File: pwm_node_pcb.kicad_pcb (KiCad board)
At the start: 4 copper layers, 40 x 35 mm, 49 parts, among them J1 Battery, J2 5V Breakout, J3 TC2050-IDC-NL, J4 CAN1, J5 Load Source, U1 LMR51430, U2 LD1117S33CTR, U3 TJA1051T/3, U4 STM32L432KCU, U5 TXB0104QPWRQ1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

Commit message: Fix level shifter circuit
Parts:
- moved C14 6.89 mm to (148.3, 111.3), turned to -90 degrees
- moved C15 6.41 mm to (148.3, 115.3), turned to 90 degrees
- moved U5 1.75 mm to (144.8, 113.3), turned to -90 degrees
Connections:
- C14 pad 1: +5V -> +3V3
- C15 pad 1: +3V3 -> +5V
- U5 pad 1: +5V -> +3V3
- U5 pad 10: /TIM1_CH1 -> /PWM2_{5V}
- U5 pad 11: /TIM1_CH4 -> /PWM3_{5V}
- U5 pad 12: /TIM1_CH3 -> /PWM4_{5V}
- U5 pad 13: /TIM1_CH2 -> /PWM1_{5V}
- U5 pad 14: +3V3 -> +5V
- U5 pad 2: /PWM2_{5V} -> /TIM1_CH1
- U5 pad 3: /PWM3_{5V} -> /TIM1_CH4
- U5 pad 4: /PWM4_{5V} -> /TIM1_CH3
- U5 pad 5: /PWM1_{5V} -> /TIM1_CH2
- U5 pad 8: +5V -> +3V3
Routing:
- net +5V: track 25.8 -> 22.8 mm, vias 8 -> 7
- net +3V3: track 25.2 -> 27.9 mm, vias 16 -> 17
- net /PWM1_{5V}: track 4.62 -> 5.67 mm
- net GND: track 27.5 -> 28.1 mm

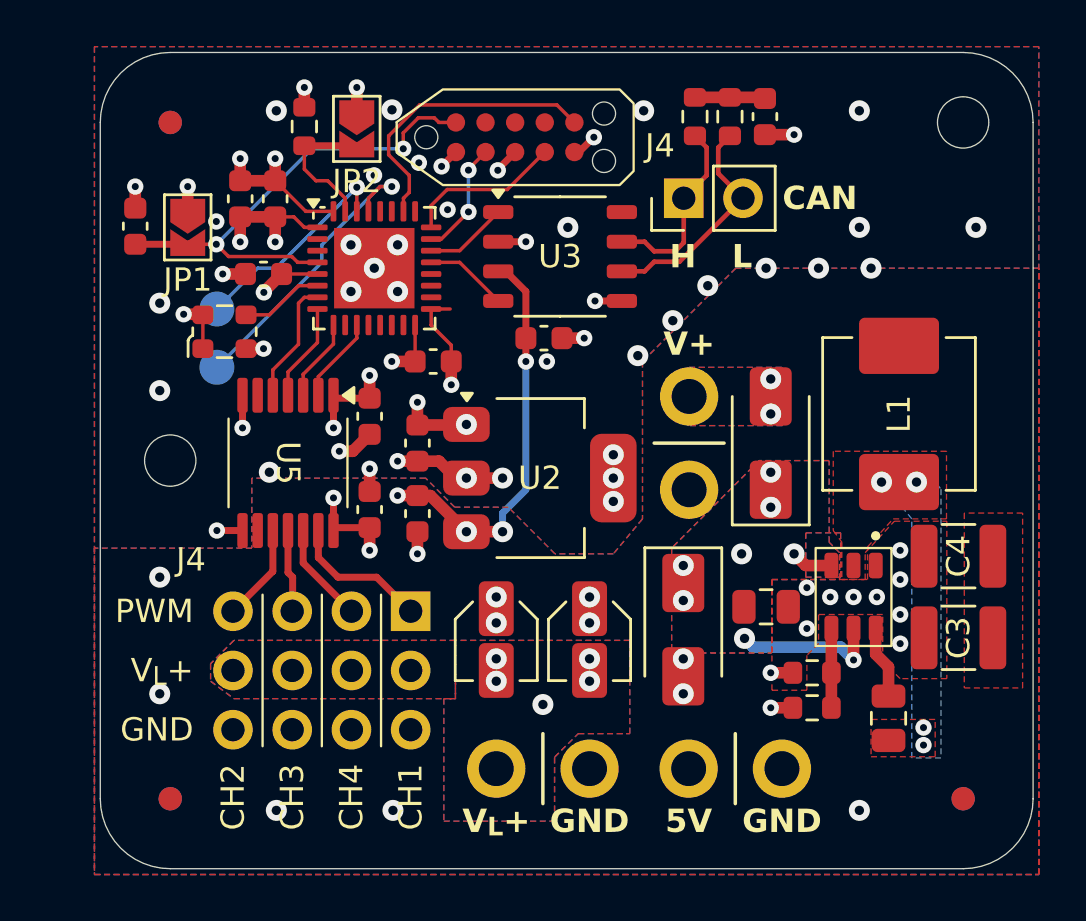
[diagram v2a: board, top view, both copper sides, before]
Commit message: Fix load cap fp and remove dedicated supply
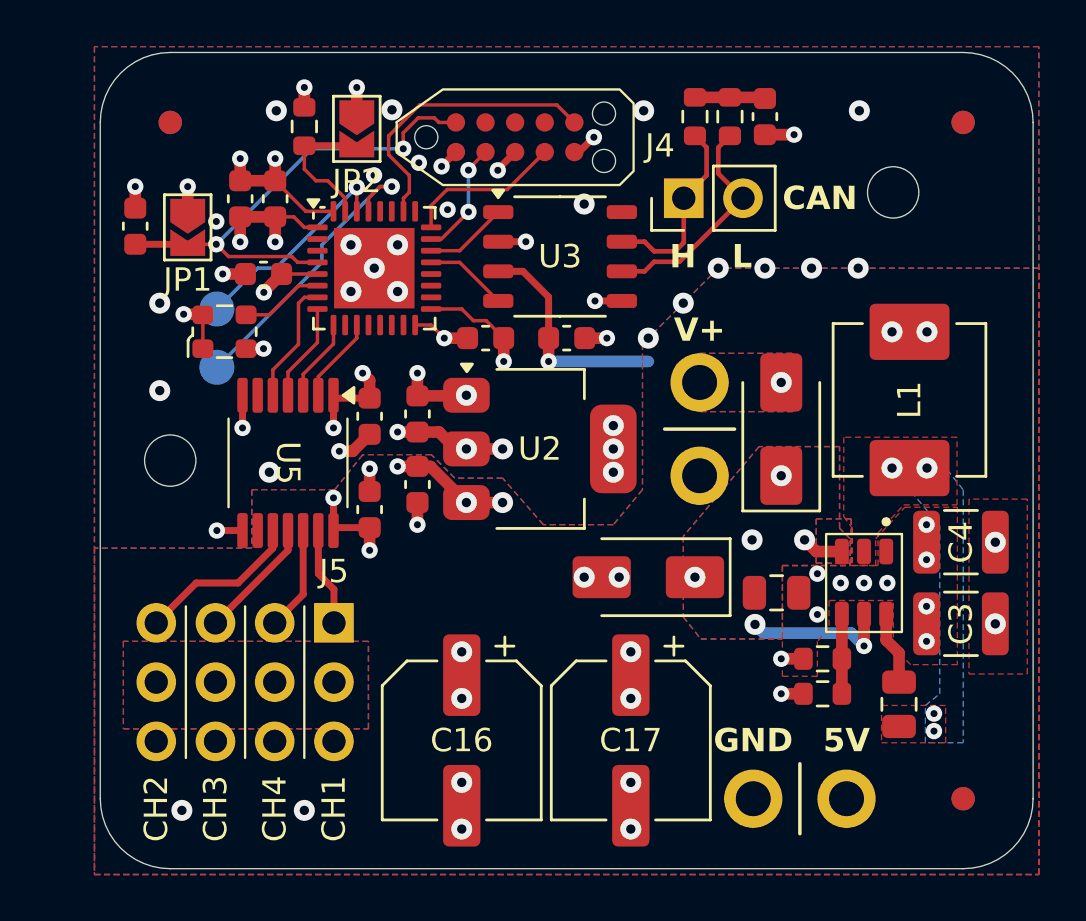
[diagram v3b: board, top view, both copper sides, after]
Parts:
- removed the J5 at (155.7, 126.5)
- C16, C17: footprint Capacitor_SMD:C_Elec_3x5.4 -> Capacitor_SMD:CP_Elec_6.3x5.2
- moved FM2 44.7 mm to (173.8, 98.8)
- moved FM5 44.7 mm to (173.8, 98.8)
- moved C17 7.21 mm to (159.5, 125.2)
- moved C16 6.98 mm to (152.2, 125.2)
- moved H2 4.24 mm to (170.8, 101.8)
- moved J5 3.33 mm to (143.0, 122.8)
- moved J2 3.06 mm to (166.8, 127.8), turned to 180 degrees
- moved D2 2.70 mm to (160.2, 118.2), turned to 180 degrees
- moved C10 2.46 mm to (153.3, 108.0)
- moved C5 1.25 mm to (150.3, 114.3)
- moved C6 1.25 mm to (150.3, 111.2)
- moved U2 1.25 mm to (155.6, 112.8)
- moved C7 0.97 mm to (156.8, 108.0)
- moved C1 0.75 mm to (171.0, 123.7)
- moved C2 0.75 mm to (165.8, 118.9)
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- renumbered J6 to J5
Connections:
- C16 pad 1: GND -> +5V
- C16 pad 2: +V_LOAD -> GND
- C17 pad 1: GND -> +5V
- C17 pad 2: +V_LOAD -> GND
- J5 pad 11: +V_LOAD -> +5V
- J5 pad 2: +V_LOAD -> +5V
- J5 pad 5: +V_LOAD -> +5V
- J5 pad 8: +V_LOAD -> +5V
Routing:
- net /PWM2_{5V}: track 4.17 -> 7.08 mm
- net +5V: track 22.8 -> 20.2 mm, vias 7 -> 15
- net /PWM3_{5V}: track 3.55 -> 5.25 mm
- net /PWM1_{5V}: track 5.67 -> 4.24 mm
- net /PWM4_{5V}: track 3.92 -> 4.47 mm
- net GND: track 28.1 -> 28.0 mm, vias 66 -> 60
- net +VSUPPLY: vias 8 -> 6
- net Net-(D1-A): vias 2 -> 1
- net +V_LOAD: vias 5 -> 0
- removed copper zone on B.Cu, net +V_LOAD
- removed copper zone on F.Cu, net +V_LOAD
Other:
- board text added: "J5"
- board text removed: "J4"
- board text removed: "V_{L}+"

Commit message: Minimize use of inpad vias
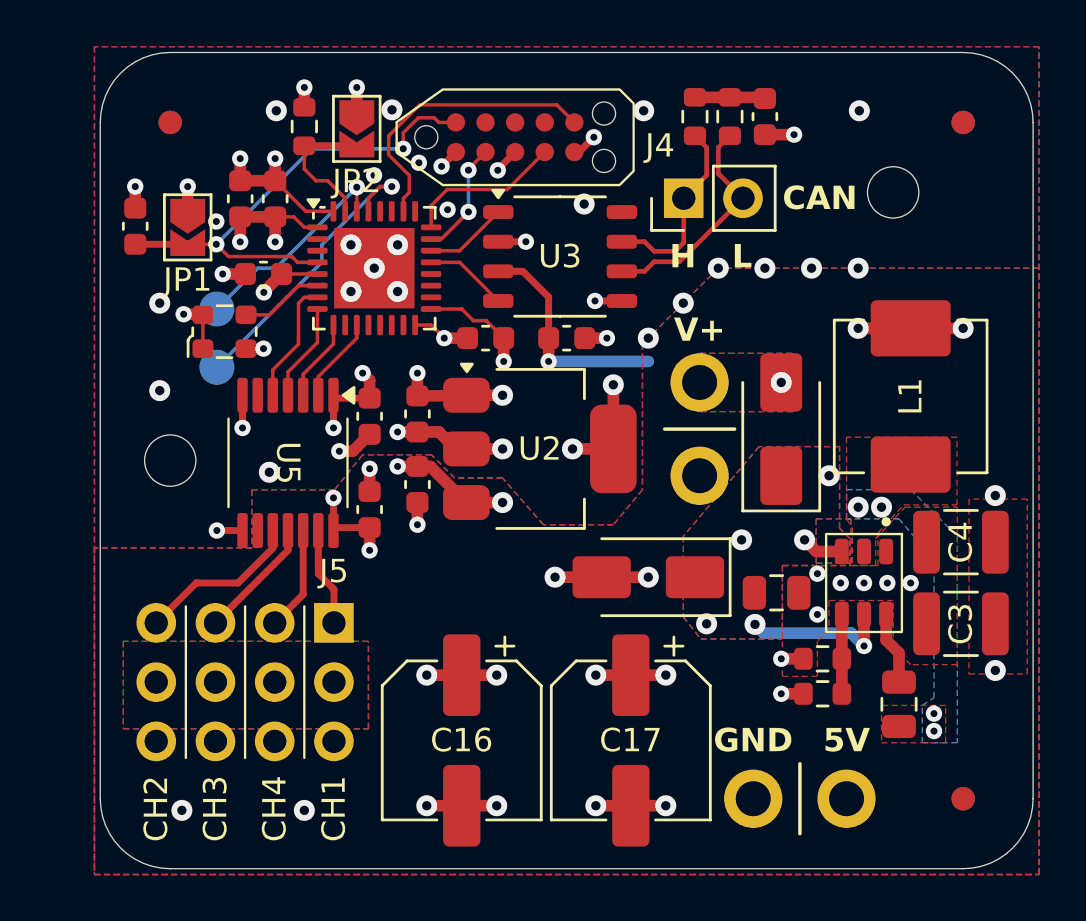
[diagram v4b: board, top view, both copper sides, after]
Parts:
- moved L1 0.16 mm to (171.5, 110.5)
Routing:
- net GND: track 28.0 -> 39.5 mm, vias 60 -> 57
- net +5V: track 20.2 -> 30.7 mm, vias 15 -> 14
- net +3V3: track 28.3 -> 32.8 mm, vias 17 -> 15

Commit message: Add TVS and schottky diode info
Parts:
- D1: value Schottky -> SK36A-LTP
- D2: value TVS -> SMAJ15A-13-F
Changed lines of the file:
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@@
 			)
 		)
-		(property "Value" "Schottky"
+		(property "Value" "SK36A-LTP"
 			(at 0 2.6 90)
 			(layer "F.Fab")
@@
 			)
 		)
-		(property "Value" "TVS"
+		(property "Value" "SMAJ15A-13-F"
 			(at 0 2.6 0)
 			(layer "F.Fab")

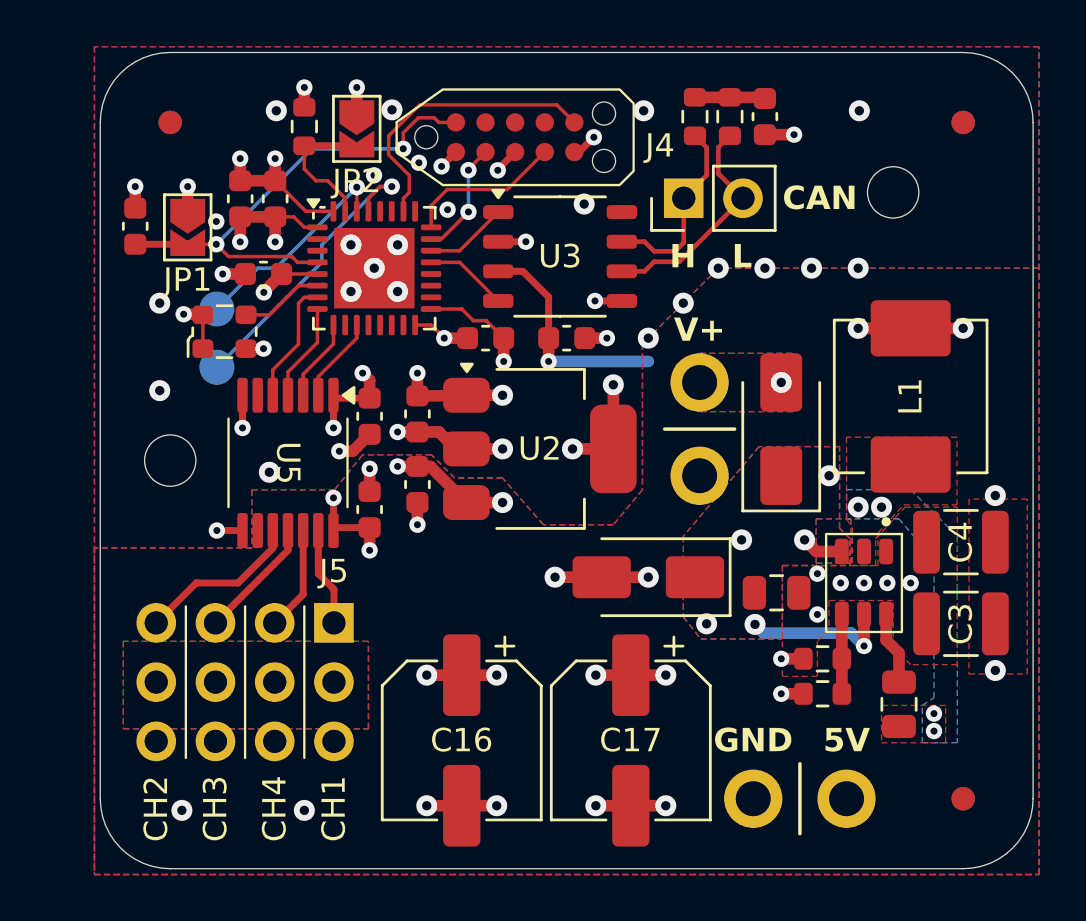
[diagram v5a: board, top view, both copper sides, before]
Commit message: Fix missing outer layer non-functional pads (vias)
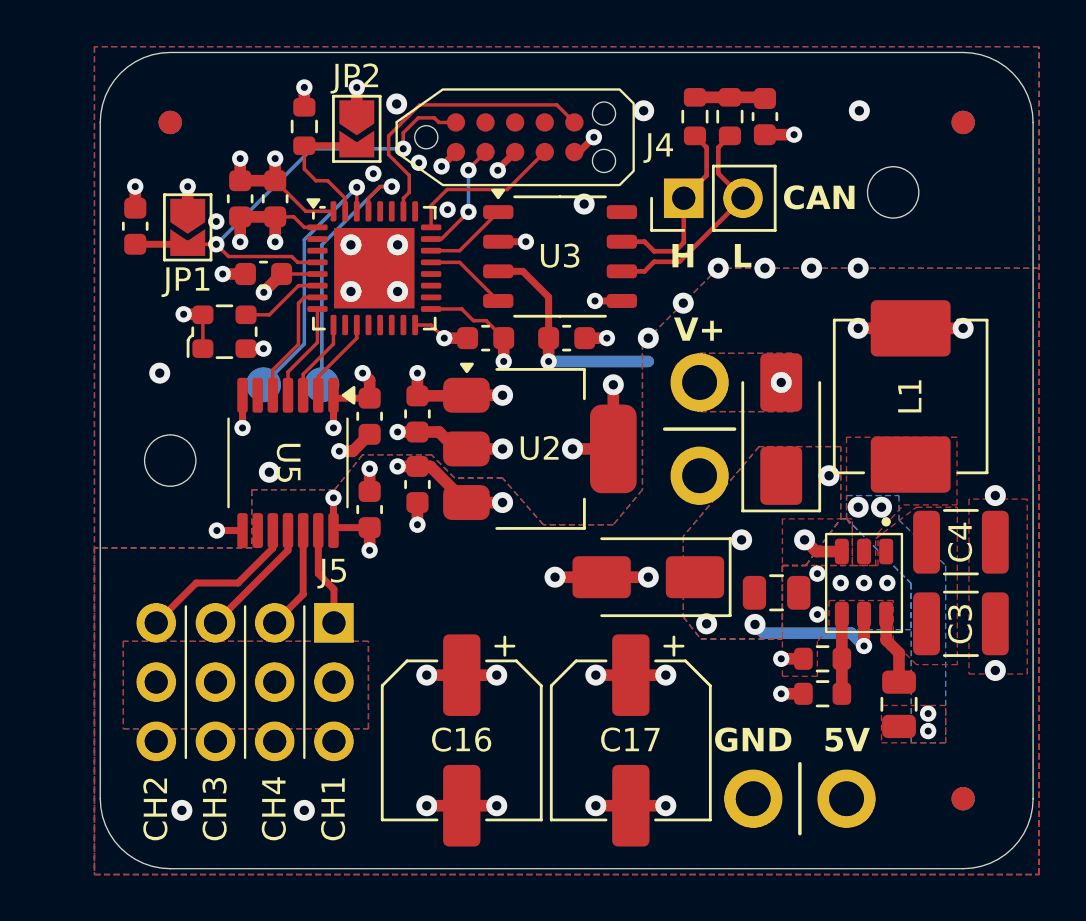
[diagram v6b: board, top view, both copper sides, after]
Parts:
- moved TP1 4.56 mm to (146.2, 110.0)
- moved TP2 3.82 mm to (143.8, 110.0)
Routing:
- net /USART1_RX: track 9.19 -> 11.2 mm
- net /USART1_TX: track 12.9 -> 11.8 mm
- net GND: vias 57 -> 53
- added copper zone on B.Cu, net GND
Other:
- board text removed: "1"
- board text removed: "2"
- board text removed: "TP"
